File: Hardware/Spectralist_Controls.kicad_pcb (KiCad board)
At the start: 2 copper layers, 60 x 110 mm, 27 parts, among them J1 Conn_01x12_Male, J10 FilterA_CV, J11 FilterB_CV, J12 ChannelAOut, J13 ChannelBOut, J14 StretchCV, J2 Conn_01x12_Male, J3 Conn_01x16_Male, J4 Conn_01x16_Male, J5 StretchCV, J6 VOctCV, J7 WarpCV, J8 PanCV, SW1 Harmonic_Switch, SW2 Filter_Switch, SW3 B_Octave

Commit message: Updates to LED board
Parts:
- SW1: footprint Custom_Footprints:SPDT_Miniature -> Custom_Footprints:SPDT_SubMiniature_Aligned
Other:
- outline, holes or cut-outs redrawn
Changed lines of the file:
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@@
 		)
 	)
-	(footprint "Custom_Footprints:SPDT_Miniature"
+	(footprint "Custom_Footprints:SPDT_SubMiniature_Aligned"
 		(layer "F.Cu")
 		(at 130 102 90)
@@
 		(tags "Switch SPDT")
 		(property "Reference" "SW1"
-			(at 0 -4.6 90)
+			(at -1.14 -3.6 90)
 			(layer "F.SilkS")
-			(hide yes)
 			(effects
 				(font
@@
 		)
 		(property "Value" "Harmonic_Switch"
-			(at 0 5.3 90)
+			(at 0 3.81 90)
 			(layer "F.Fab")
 			(effects
@@
 			)
 		)
-		(property "Footprint" "Custom_Footprints:SPDT_Miniature"
+		(property "Footprint" "Custom_Footprints:SPDT_SubMiniature_Aligned"
 			(at 0 0 90)
 			(layer "F.Fab")
@@
 		(sheetfile "Spectralist_Controls.kicad_sch")
 		(attr through_hole)
-		(fp_rect
-			(start -6.4 -3.45)
-			(end 6.4 3.45)
+		(fp_line
+			(start -4.1034 -2.681)
+			(end 4.064 -2.681)
 			(stroke
-				(width 0.12)
-				(type default)
+				(width 0.15)
+				(type solid)
 			)
-			(fill none)
 			(layer "F.SilkS")
 		)
-		(fp_circle
-			(center 0 0)
-			(end 3.175 0)
+		(fp_line
+			(start 1.714 2.681)
+			(end 4.014 2.681)
 			(stroke
-				(width 0.12)
-				(type default)
+				(width 0.15)
+				(type solid)
 			)
-			(fill none)
-			(layer "Dwgs.User")
+			(layer "F.SilkS")
 		)
-		(fp_rect
-			(start -6.5 -3.55)
-			(end 6.5 3.55)
+		(fp_line
+			(start -4.078 2.681)
+			(end -1.878 2.681)
 			(stroke
-				(width 0.12)
-				(type default)
+				(width 0.15)
+				(type solid)
+			)
+			(layer "F.SilkS")
+		)
+		(fp_line
+			(start 4.1948 -2.7254)
+			(end 4.191 2.763)
+			(stroke
+				(width 0.05)
+				(type solid)
 			)
-			(fill none)
 			(layer "F.CrtYd")
 		)
+		(fp_line
+			(start -4.1826 -2.7254)
+			(end 4.1948 -2.7254)
+			(stroke
+				(width 0.05)
+				(type solid)
+			)
+			(layer "F.CrtYd")
+		)
+		(fp_line
+			(start 4.191 2.763)
+			(end -4.1826 2.763)
+			(stroke
+				(width 0.05)
+				(type solid)
+			)
+			(layer "F.CrtYd")
+		)
+		(fp_line
+			(start -4.1826 2.763)
+			(end -4.1826 -2.7254)
+			(stroke
+				(width 0.05)
+				(type solid)
+			)
+			(layer "F.CrtYd")
+		)
+		(fp_line
+			(start 4.064 -2.54)
+			(end 4.064 2.54)
+			(stroke
+				(width 0.1)
+				(type solid)
+			)
+			(layer "F.Fab")
+		)
+		(fp_line
+			(start -4.064 -2.54)
+			(end 4.064 -2.54)
+			(stroke
+				(width 0.1)
+				(type solid)
+			)
+			(layer "F.Fab")
+		)
+		(fp_line
+			(start -4.064 -2.54)
+			(end -4.064 2.54)
+			(stroke
+				(width 0.1)
+				(type solid)
+			)
+			(layer "F.Fab")
+		)
+		(fp_line
+			(start -4.064 2.54)
+			(end 4.064 2.54)
+			(stroke
+				(width 0.1)
+				(type solid)
+			)
+			(layer "F.Fab")
+		)
 		(fp_text user "${REFERENCE}"
-			(at 0 2.6 90)
+			(at -0.24 1.7 90)
 			(layer "F.Fab")
-			(hide yes)
 			(effects
 				(font
@@
 			)
 		)
-		(pad "1" thru_hole circle
-			(at -4.7 0 90)
-			(size 3 3)
-			(drill 1.85)
+		(pad "1" thru_hole rect
+			(at -2.54 0 90)
+			(size 1.5 2.5)
+			(drill 1.0922)
 			(layers "*.Cu" "*.Mask")
 			(remove_unused_layers no)
@@
 			(pintype "passive")
 		)
-		(pad "2" thru_hole circle
+		(pad "2" thru_hole oval
 			(at 0 0 90)
-			(size 3 3)
-			(drill 1.85)
+			(size 1.5 2.5)
+			(drill 1.0922)
 			(layers "*.Cu" "*.Mask")
 			(remove_unused_layers no)
@@
 			(pintype "passive")
 		)
-		(pad "3" thru_hole circle
-			(at 4.7 0 90)
-			(size 3 3)
-			(drill 1.85)
+		(pad "3" thru_hole oval
+			(at 2.54 0 90)
+			(size 1.5 2.5)
+			(drill 1.0922)
 			(layers "*.Cu" "*.Mask")
 			(remove_unused_layers no)
@@
 			(pintype "passive")
 		)
-		(model "${CUSTOM_3D}/SPDT_Toggle_Switch.step"
+		(model "${CUSTOM_3D}/Toggle Switch Daily Well 1AS1T2B4M2QE.STEP"
 			(offset
-				(xyz 0 0 0)
+				(xyz 0 0 8)
 			)
 			(scale
-				(xyz 1 1 1)
+				(xyz 0.55 0.55 0.8)
 			)
 			(rotate
-				(xyz -90 0 0)
+				(xyz 0 0 0)
 			)
 		)
@@
 		(tags "Potentiometer 9mm")
 		(property "Reference" "Stretch_Trim1"
-			(at -0.04 10.04 360)
+			(at -0.04 10.04 0)
 			(layer "F.SilkS")
 			(effects
@@
 		)
 		(property "Value" "B10k"
-			(at -0.2 -7.4 360)
+			(at -0.2 -7.4 0)
 			(layer "F.Fab")
 			(effects
@@
 		)
 		(property "Footprint" "Custom_Footprints:Alpha_9mm_Potentiometer_Aligned"
-			(at 0 0 360)
+			(at 0 0 0)
 			(layer "F.Fab")
 			(hide yes)
@@
 		)
 		(property "Datasheet" ""
-			(at 0 0 360)
+			(at 0 0 0)
 			(layer "F.Fab")
 			(hide yes)
@@
 		)
 		(property "Description" "Potentiometer"
-			(at 0 0 360)
+			(at 0 0 0)
 			(layer "F.Fab")
 			(hide yes)
@@
 		(tags "LED diameter 3.0mm 2 pins")
 		(property "Reference" "D3"
-			(at 0 -2.96 360)
+			(at 0 -2.96 0)
 			(layer "F.SilkS")
 			(hide yes)
@@
 		)
 		(property "Value" "OctLED"
-			(at 0 2.96 360)
+			(at 0 2.96 0)
 			(layer "F.Fab")
 			(effects
@@
 		)
 		(property "Footprint" "Custom_Footprints:LED_D3.0mm"
-			(at 0 0 360)
+			(at 0 0 0)
 			(layer "F.Fab")
 			(hide yes)
@@
 		)
 		(property "Datasheet" ""
-			(at 0 0 360)
+			(at 0 0 0)
 			(layer "F.Fab")
 			(hide yes)
@@
 		)
 		(property "Description" "Light emitting diode, small symbol"
-			(at 0 0 360)
+			(at 0 0 0)
 			(layer "F.Fab")
 			(hide yes)
@@
 		(tags "tact sw push 6mm")
 		(property "Reference" "SW3"
-			(at 0 -4.25 360)
+			(at 0 -4.25 0)
 			(layer "F.SilkS")
 			(effects
@@
 		)
 		(property "Value" "B_Octave"
-			(at 0 5.45 360)
+			(at 0 5.45 0)
 			(layer "F.Fab")
 			(effects
@@
 		)
 		(property "Footprint" "Custom_Footprints:SW_PUSH_6mm_aligned"
-			(at 0 0 360)
+			(at 0 0 0)
 			(layer "F.Fab")
 			(hide yes)
@@
 		)
 		(property "Datasheet" ""
-			(at 0 0 360)
+			(at 0 0 0)
 			(layer "F.Fab")
 			(hide yes)
@@
 		)
 		(property "Description" "Push button switch, generic, two pins"
-			(at 0 0 360)
+			(at 0 0 0)
 			(layer "F.Fab")
 			(hide yes)
@@
 	(gr_poly
 		(pts
-			(xy 114 82) (xy 146 82) (xy 146 115) (xy 142 115) (xy 142 119) (xy 118 119) (xy 118 115) (xy 114 115)
+			(xy 110 101) (xy 114 101) (xy 114 92) (xy 114 82) (xy 146 82) (xy 146 101) (xy 150 101) (xy 150 115)
+			(xy 142 115) (xy 142 119) (xy 118 119) (xy 118 115) (xy 110 115)
 		)
 		(stroke

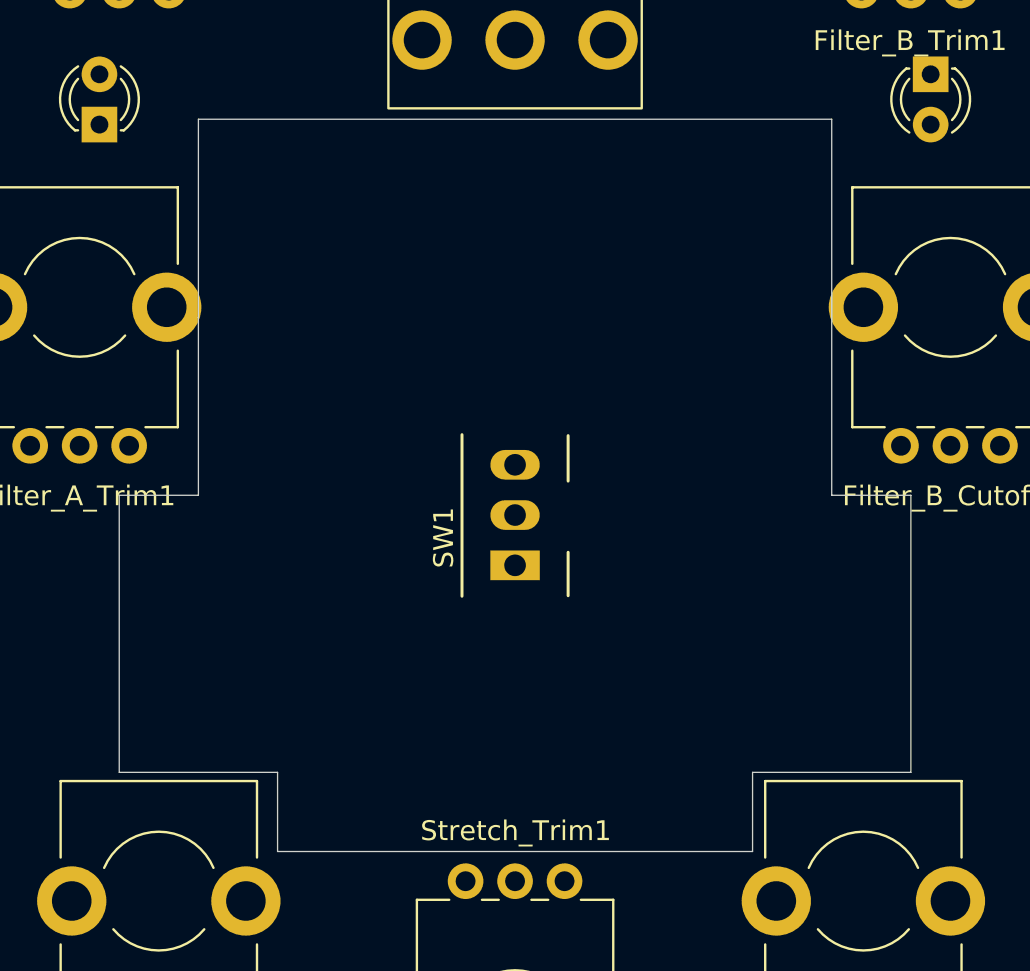
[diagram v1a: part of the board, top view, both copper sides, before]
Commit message: Curvy traces on LED board
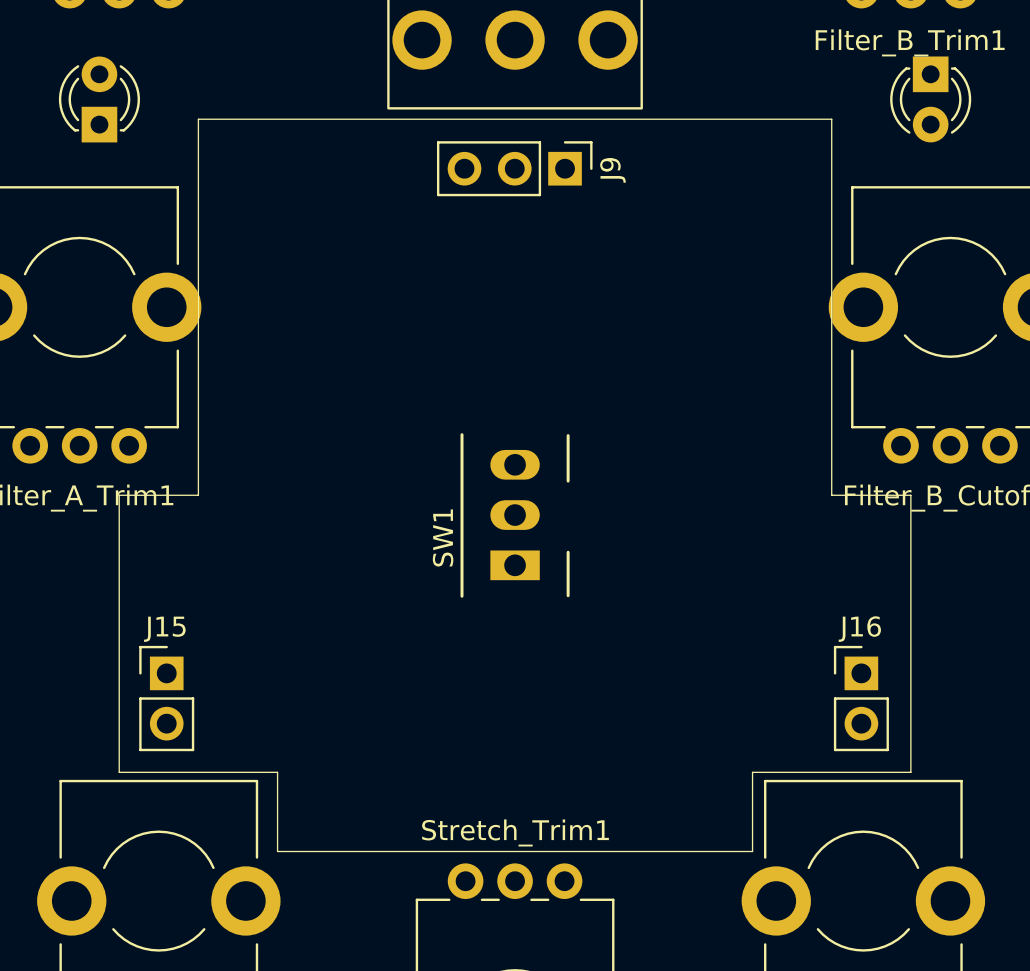
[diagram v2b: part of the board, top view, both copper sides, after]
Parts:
- added J15: Conn_01x02_Pin, Connector_PinHeader_2.54mm:PinHeader_1x02_P2.54mm_Vertical, F.Cu at (112.4, 110.0)
- added J16: Conn_01x02_Pin, Connector_PinHeader_2.54mm:PinHeader_1x02_P2.54mm_Vertical, F.Cu at (147.5, 110.0)
- added J9: Conn_01x03_Pin, Connector_PinHeader_2.54mm:PinHeader_1x03_P2.54mm_Vertical, F.Cu at (132.5, 84.5)
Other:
- outline, holes or cut-outs redrawn

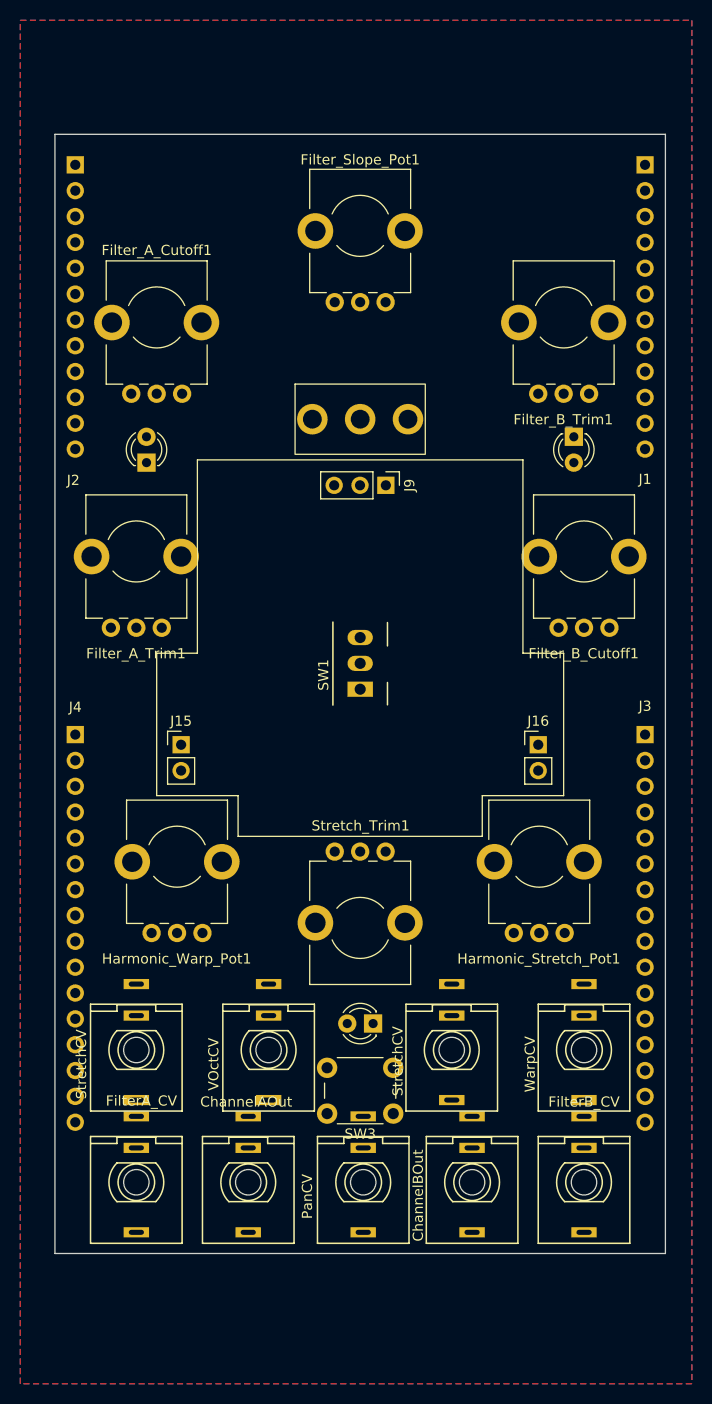
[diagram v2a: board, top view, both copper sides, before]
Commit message: Component PCB updates
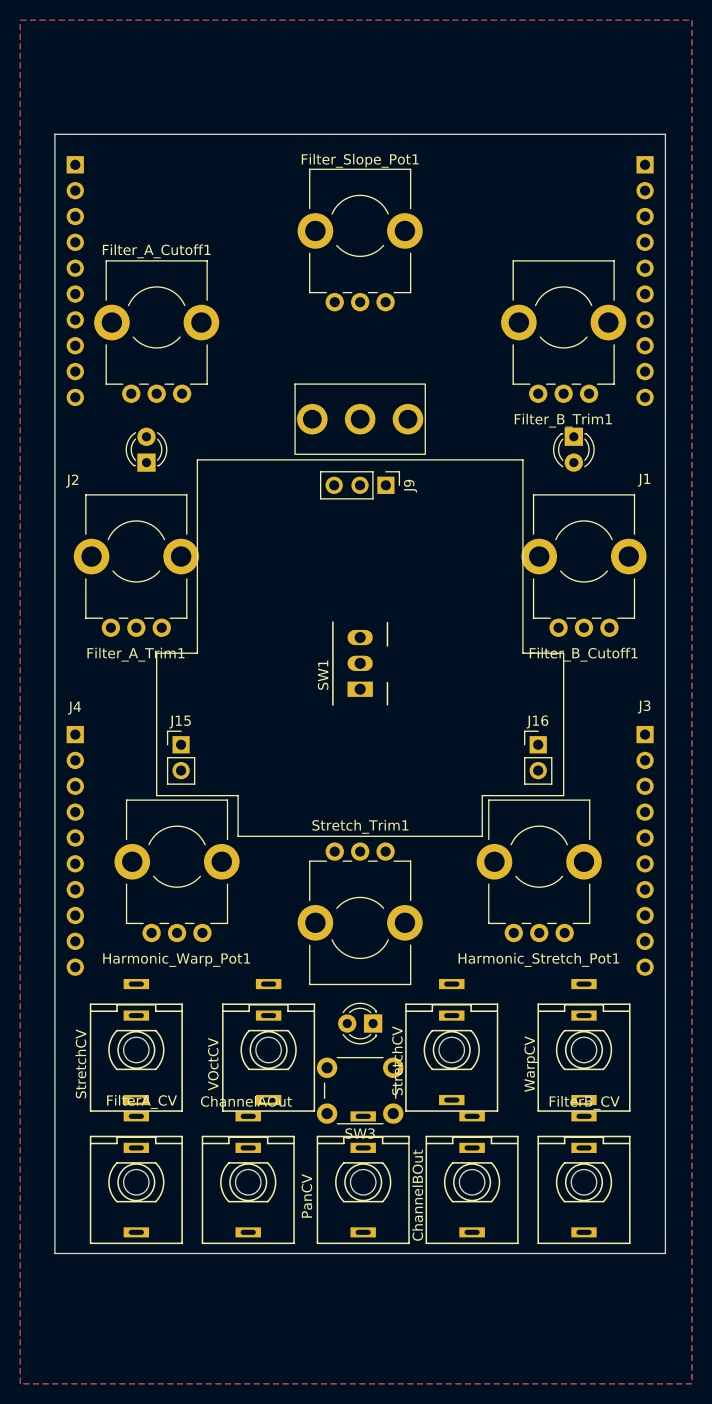
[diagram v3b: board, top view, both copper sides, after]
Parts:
- J1, J2: value Conn_01x12_Male -> Conn_01x10_Pin; footprint Connector_PinSocket_2.54mm:PinSocket_1x12_P2.54mm_Vertical -> Connector_PinHeader_2.54mm:PinHeader_1x10_P2.54mm_Vertical
- J3, J4: value Conn_01x16_Male -> Conn_01x10_Pin; footprint Connector_PinSocket_2.54mm:PinSocket_1x16_P2.54mm_Vertical -> Connector_PinHeader_2.54mm:PinHeader_1x10_P2.54mm_Vertical
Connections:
- net /FM2_Out renamed /Filter_A_CV_In
- net /Gate_Normal renamed /Filter_A_Pot
- net /Ramp_LED renamed /LED_Oct_Out
- net /Ramp_Out renamed /Filter_A_Trm
- net /Sine1_Inv_Out renamed /I2C5_SCL
- net /Sine1_LED renamed /Pitch_CV_In
- net /Sine1_Out renamed /I2C5_SDA
- net /Sine1_Ramp_Lvl_LED renamed /Harm_Warp_Pot
- net /Sine1_Swell_Rate_LED renamed /Harm_Stretch_Trm
- net /Sine2_LED renamed /Harm_Stretch_Pot
- net /Sine2_Level renamed /Filter_B_CV_In
- net /Sine2_Out renamed /Filter_Mode
- net /Sine2_Ramp_Lvl_LED renamed /Harm_Warp_CV_In
- net /Sine2_Ramp_Rate_LED renamed /LED_Filter_A_Out
- net /Sine3_LED renamed /LED_Filter_B_Out
- net /Sine3_Out renamed /Warp_Mode
- net /Sine3_Ramp_Lvl_LED renamed /Pan_CV_In
- net /Swell_Level renamed /Filter_B_Trm
- net /Swell_Out renamed /Filter_B_Pot
- net /Swell_Rate renamed /Harm_Stretch_CV_In
- J1 pad 1: GND -> /Filter_Slope_Pot
- J1 pad 10: GND -> unconnected-(J1-Pin_10-Pad10)
- J1 pad 2: /FM3_Out -> GND
- J1 pad 6: /Sine1_Level -> GND
- J1 pad 9: /Ramp_Rate -> unconnected-(J1-Pin_9-Pad9)
- J2 pad 10: GND -> unconnected-(J2-Pin_10-Pad10)
- J2 pad 3: GND -> +12V
- J2 pad 6: /Sine3_Level -> GND
- J2 pad 9: +3.3VA -> unconnected-(J2-Pin_9-Pad9)
- J3 pad 10: /Sine3_Swell_Lvl_LED -> unconnected-(J3-Pin_10-Pad10)
- J3 pad 3: /Sine3_Ramp_Rate_LED -> unconnected-(J3-Pin_3-Pad3)
- J3 pad 6: GND -> /Filter_Slope_CV_In
- J3 pad 8: /Sine1_Swell_Lvl_LED -> unconnected-(J3-Pin_8-Pad8)
- J3 pad 9: /Sine2_Swell_Lvl_LED -> unconnected-(J3-Pin_9-Pad9)
- J4 pad 1: /Sine3_Swell_Rate_LED -> /Octave_Btn
- J4 pad 10: /Sine2_Rate_Btn -> unconnected-(J4-Pin_10-Pad10)
- J4 pad 4: /Swell_LED -> unconnected-(J4-Pin_4-Pad4)
- J4 pad 8: GND -> unconnected-(J4-Pin_8-Pad8)
- J4 pad 9: /Sine3_Rate_Btn -> unconnected-(J4-Pin_9-Pad9)

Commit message: More layout on Component and Control boards
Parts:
- J1, J2: value Conn_01x10_Pin -> Conn_01x8_Pin; footprint Connector_PinHeader_2.54mm:PinHeader_1x10_P2.54mm_Vertical -> Connector_PinHeader_2.54mm:PinHeader_1x08_P2.54mm_Vertical
- J14: value StretchCV -> SlopeCV
- moved J3 10.0 mm to (158.0, 119.0)
- moved J4 10.0 mm to (102.0, 119.0)
- moved J1 5.00 mm to (158.0, 58.0)
- moved J2 5.00 mm to (102.0, 58.0)
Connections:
- D1 pad 2: /Filter_A_LED -> /LED_Filter_A_Out
- D2 pad 2: /Filter_B_LED -> /LED_Filter_B_Out
- D3 pad 2: /Octave_LED -> /LED_Oct_Out
- Filter_A_Cutoff1 pad 2: /Filter_A_Cutoff -> /Filter_A_Pot
- Filter_A_Trim1 pad 2: /Filter_A_Trim -> /Filter_A_Trm
- Filter_B_Cutoff1 pad 2: /Filter_B_Cutoff -> /Filter_B_Pot
- Filter_B_Trim1 pad 2: /Filter_B_Trim -> /Filter_B_Trm
- Filter_Slope_Pot1 pad 2: /Filter_Slope -> /Filter_Slope_Pot
- Harmonic_Stretch_Pot1 pad 2: /Harmonic_Stretch -> /Harm_Stretch_Pot
- Harmonic_Warp_Pot1 pad 2: /Harmonic_Warp -> /Harm_Warp_Pot
- J1 pad 1: /Filter_Slope_Pot -> GND
- J1 pad 2: GND -> /LED_SCL
- J1 pad 3: /Filter_A_CV_In -> /LED_SDA
- J1 pad 4: /Filter_A_Trm -> GND
- J1 pad 5: /Filter_B_Pot -> /LED_Filter_A_Out
- J1 pad 6: GND -> /LED_Oct_Out
- J1 pad 7: /Filter_B_CV_In -> /LED_Filter_B_Out
- J1 pad 8: /Filter_B_Trm -> GND
- J10 pad 3: /Filter_A_In -> /Filter_A_CV_In
- J11 pad 3: /Filter_B_In -> /Filter_B_CV_In
- J12 pad 3: /Channel_A_Out -> /Audio_Out_L
- J13 pad 3: /Channel_B_Out -> /Audio_Out_R
- J14 pad 3: /Stretch_In -> /Filter_Slope_CV_In
- J2 pad 1: /Filter_A_Pot -> +3.3V
- J2 pad 2: +3.3V -> /Filter_Mode
- J2 pad 3: +12V -> /Harmonic_Mode
- J2 pad 4: /Filter_Mode -> GND
- J2 pad 5: /Warp_Mode -> /Octave_Btn
- J2 pad 6: GND -> /Filter_A_Pot
- J2 pad 7: /I2C5_SDA -> /Filter_A_Trm
- J2 pad 8: /I2C5_SCL -> +12V
- J3 pad 1: /Harm_Stretch_Trm -> /Filter_B_Trm
- J3 pad 10: unconnected-(J3-Pin_10-Pad10) -> /Harm_Warp_Pot
- J3 pad 2: /Harm_Stretch_CV_In -> /Audio_Out_L
- J3 pad 3: unconnected-(J3-Pin_3-Pad3) -> GND
- J3 pad 4: /Harm_Warp_Pot -> /Audio_Out_R
- J3 pad 5: /Harm_Warp_CV_In -> /Filter_Slope_Pot
- J3 pad 6: /Filter_Slope_CV_In -> /Filter_B_Pot
- J3 pad 7: /Pan_CV_In -> GND
- J3 pad 8: unconnected-(J3-Pin_8-Pad8) -> /Harm_Stretch_Trm
- J3 pad 9: unconnected-(J3-Pin_9-Pad9) -> /Harm_Stretch_Pot
- J4 pad 1: /Octave_Btn -> GND
- J4 pad 10: unconnected-(J4-Pin_10-Pad10) -> /Filter_A_CV_In
- J4 pad 2: /Harm_Stretch_Pot -> /Harm_Warp_CV_In
- J4 pad 3: /Pitch_CV_In -> /Filter_B_CV_In
- J4 pad 4: unconnected-(J4-Pin_4-Pad4) -> GND
- J4 pad 5: /LED_Oct_Out -> /Filter_Slope_CV_In
- J4 pad 6: /LED_Filter_A_Out -> /Pan_CV_In
- J4 pad 7: /LED_Filter_B_Out -> GND
- J4 pad 8: unconnected-(J4-Pin_8-Pad8) -> /Pitch_CV_In
- J4 pad 9: unconnected-(J4-Pin_9-Pad9) -> /Harm_Stretch_CV_In
- J5 pad 3: /Stretch_In -> /Harm_Stretch_CV_In
- J6 pad 3: /V_Oct_In -> /Pitch_CV_In
- J7 pad 3: /Warp_In -> /Harm_Warp_CV_In
- J8 pad 3: /Pan_In -> /Pan_CV_In
- SW2 pad 2: /Filter_Type -> /Filter_Mode
- Stretch_Trim1 pad 2: /Stretch_Trim -> /Harm_Stretch_Trm
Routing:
- net +3.3VA: track 0.00 -> 186.5 mm
- net /Octave_Btn: track 0.00 -> 92.0 mm
- net +3.3V: track 0.00 -> 85.3 mm
- net /LED_Oct_Out: track 0.00 -> 81.8 mm
- net /Filter_Slope_Pot: track 0.00 -> 77.5 mm
- net /Filter_B_CV_In: track 0.00 -> 67.3 mm
- net /Harm_Warp_CV_In: track 0.00 -> 62.2 mm
- net /LED_Filter_A_Out: track 0.00 -> 60.6 mm
- net /Audio_Out_L: track 0.00 -> 58.4 mm
- net /Harm_Warp_Pot: track 0.00 -> 52.9 mm
- net /Harmonic_Mode: track 0.00 -> 52.4 mm
- net /Filter_B_Trm: track 0.00 -> 47.7 mm
- net /Filter_Slope_CV_In: track 0.00 -> 43.5 mm
- net +12V: track 0.00 -> 43.3 mm
- net /Pan_CV_In: track 0.00 -> 42.9 mm
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
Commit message: More PCB Layout
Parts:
- moved SW3 2.00 mm to (130.0, 142.0)
- moved D3 1.40 mm to (130.0, 136.0)
- moved J14 1.00 mm to (140.0, 140.0)
- moved J6 1.00 mm to (120.0, 140.0)
- moved Stretch_Trim1 1.00 mm to (130.0, 127.0)
- moved J8 0.30 mm to (130.0, 153.0)
- renumbered Filter_B_Trim1 to Filter_B_Cutoff1, Filter_B_Cutoff1 to Filter_B_Trim1
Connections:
- Filter_B_Cutoff1 pad 2: /Filter_B_Trm -> /Filter_B_Pot
- Filter_B_Trim1 pad 2: /Filter_B_Pot -> /Filter_B_Trm
- J1 pad 7: /LED_Filter_B_Out -> GND
- J1 pad 8: GND -> /LED_Filter_B_Out
- J3 pad 1: /Filter_B_Trm -> /Filter_B_Pot
- J3 pad 6: /Filter_B_Pot -> /Filter_B_Trm
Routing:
- net /Filter_B_Trm: track 47.7 -> 35.7 mm
- net /Filter_B_Pot: track 35.7 -> 47.7 mm
- net /Audio_Out_L: track 58.4 -> 65.8 mm
- net /Octave_Btn: track 92.0 -> 97.6 mm
- net /Harm_Stretch_Pot: track 19.2 -> 16.2 mm
- net +12V: track 43.3 -> 41.1 mm
- net /LED_Filter_B_Out: track 11.9 -> 9.69 mm
- net /Harm_Stretch_Trm: track 37.1 -> 39.3 mm
- net +3.3VA: track 186.5 -> 184.4 mm
- net /Harm_Warp_CV_In: track 62.2 -> 60.6 mm
- net /Filter_Slope_CV_In: track 43.5 -> 44.5 mm
- net /Pitch_CV_In: track 22.4 -> 21.4 mm
- net +3.3V: track 85.3 -> 84.4 mm
- net /LED_Oct_Out: track 81.8 -> 81.2 mm
